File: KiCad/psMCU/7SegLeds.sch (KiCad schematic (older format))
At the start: 14 parts

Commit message: First Schematic Draft done.
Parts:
- removed D? (x6): LED, Diode_SMD:D_0603_1608Metric, symbol Device:LED_Small
- added D34, D35, D37, D38, D39, D40: LED_7seg, NoRef_Footprints:D_0402_1005Metric_NoRef, symbol Device:LED_Small
- D36: renamed from D?; value LED -> LED_7seg; footprint Diode_SMD:D_0603_1608Metric -> NoRef_Footprints:D_0402_1005Metric_NoRef
- R36, R37, R38, R39, R40, R41, R42: renamed from R?; footprint Resistor_SMD:R_0603_1608Metric -> NoRef_Footprints:R_0603_1608Metric
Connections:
- net GND: now also D34.1 (K), D35.1 (K), D37.1 (K), D38.1 (K), D39.1 (K), D40.1 (K)
- net at R37.1: now also D35.2 (A)
- net at R41.1: now also D39.2 (A)
- net at R40.1: now also D38.2 (A)
- net at R36.1: now also D34.2 (A)
- net at R39.1: now also D37.2 (A)
- net at R42.1: now also D40.2 (A)
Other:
- moved on the sheet: R360

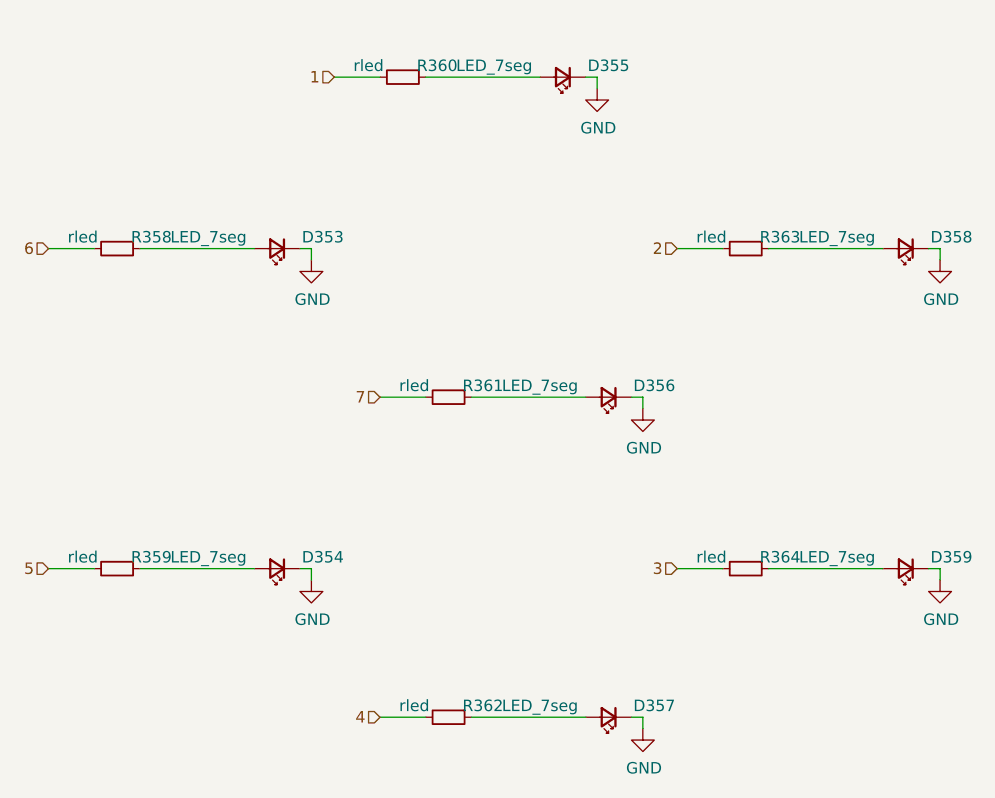
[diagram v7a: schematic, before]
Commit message: Reworked ref. location in schematic.
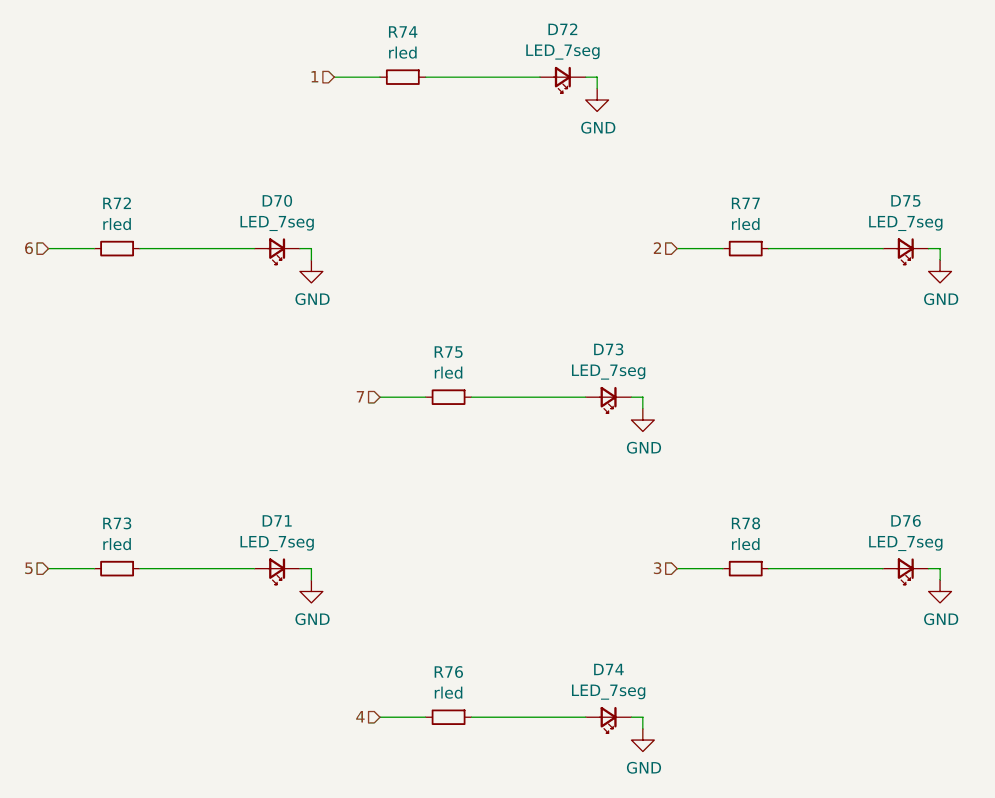
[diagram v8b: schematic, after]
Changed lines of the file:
@@
 $Descr A4 11693 8268
 encoding utf-8
-Sheet 82 110
+Sheet 19 110
 Title "psMCU"
 Date ""
@@
 AR Path="/5F607AA2/6046BFE9/61AA9AC0/607AED25" Ref="#PWR0512"  Part="1"
 AR Path="/5F607AA2/6046BFE9/61AA9AC7/607AED25" Ref="#PWR0526"  Part="1"
-F 0 "#PWR01202" H 6550 2000 50  0001 C CNN
+F 0 "#PWR0346" H 6550 2000 50  0001 C CNN
 F 1 "GND" H 6555 2077 50  0000 C CNN
 F 2 "" H 6550 2250 50  0001 C CNN
@@
 AR Path="/5F607AA2/6046BFE9/61AA9AC0/607AED30" Ref="R133"  Part="1"
 AR Path="/5F607AA2/6046BFE9/61AA9AC7/607AED30" Ref="R147"  Part="1"
-F 0 "R361" V 5850 3750 50  0000 C CNN
-F 1 "rled" V 5850 3450 50  0000 C CNN
+F 0 "R75" V 5704 3600 50  0000 C CNN
+F 1 "rled" V 5795 3600 50  0000 C CNN
 F 2 "NoRef_Footprints:R_0603_1608Metric" H 5900 3600 50  0001 C CNN
 F 3 "~" H 5900 3600 50  0001 C CNN
@@
 AR Path="/5F607AA2/6046BFE9/61AA9AC0/607AED32" Ref="R136"  Part="1"
 AR Path="/5F607AA2/6046BFE9/61AA9AC7/607AED32" Ref="R150"  Part="1"
-F 0 "R364" V 7150 4500 50  0000 C CNN
-F 1 "rled" V 7150 4200 50  0000 C CNN
+F 0 "R78" V 7004 4350 50  0000 C CNN
+F 1 "rled" V 7095 4350 50  0000 C CNN
 F 2 "NoRef_Footprints:R_0603_1608Metric" H 7200 4350 50  0001 C CNN
 F 3 "~" H 7200 4350 50  0001 C CNN
@@
 AR Path="/5F607AA2/6046BFE9/61AA9AC0/607AED35" Ref="R134"  Part="1"
 AR Path="/5F607AA2/6046BFE9/61AA9AC7/607AED35" Ref="R148"  Part="1"
-F 0 "R362" V 5850 5150 50  0000 C CNN
-F 1 "rled" V 5850 4850 50  0000 C CNN
+F 0 "R76" V 5704 5000 50  0000 C CNN
+F 1 "rled" V 5795 5000 50  0000 C CNN
 F 2 "NoRef_Footprints:R_0603_1608Metric" H 5900 5000 50  0001 C CNN
 F 3 "~" H 5900 5000 50  0001 C CNN
@@
 AR Path="/5F607AA2/6046BFE9/61AA9AC0/607AED37" Ref="R130"  Part="1"
 AR Path="/5F607AA2/6046BFE9/61AA9AC7/607AED37" Ref="R144"  Part="1"
-F 0 "R358" V 4400 3100 50  0000 C CNN
-F 1 "rled" V 4400 2800 50  0000 C CNN
+F 0 "R72" V 4254 2950 50  0000 C CNN
+F 1 "rled" V 4345 2950 50  0000 C CNN
 F 2 "NoRef_Footprints:R_0603_1608Metric" H 4450 2950 50  0001 C CNN
 F 3 "~" H 4450 2950 50  0001 C CNN
@@
 AR Path="/5F607AA2/6046BFE9/61AA9AC0/6039674B" Ref="R131"  Part="1"
 AR Path="/5F607AA2/6046BFE9/61AA9AC7/6039674B" Ref="R145"  Part="1"
-F 0 "R359" V 4400 4500 50  0000 C CNN
-F 1 "rled" V 4400 4200 50  0000 C CNN
+F 0 "R73" V 4254 4350 50  0000 C CNN
+F 1 "rled" V 4345 4350 50  0000 C CNN
 F 2 "NoRef_Footprints:R_0603_1608Metric" H 4450 4350 50  0001 C CNN
 F 3 "~" H 4450 4350 50  0001 C CNN
@@
 AR Path="/5F607AA2/6046BFE9/61AA9AC0/607AED24" Ref="D127"  Part="1"
 AR Path="/5F607AA2/6046BFE9/61AA9AC7/607AED24" Ref="D141"  Part="1"
-F 0 "D355" H 6200 2150 50  0000 C CNN
-F 1 "LED_7seg" H 6700 2150 50  0000 C CNN
+F 0 "D72" H 6400 1993 50  0000 C CNN
+F 1 "LED_7seg" H 6400 2084 50  0000 C CNN
 F 2 "NoRef_Footprints:D_0402_1005Metric_NoRef" V 6400 2200 50  0001 C CNN
 F 3 "~" V 6400 2200 50  0001 C CNN
@@
 AR Path="/5F607AA2/6046BFE9/61AA9AC0/607AED2A" Ref="R132"  Part="1"
 AR Path="/5F607AA2/6046BFE9/61AA9AC7/607AED2A" Ref="R146"  Part="1"
-F 0 "R360" V 5650 2350 50  0000 C CNN
-F 1 "rled" V 5650 2050 50  0000 C CNN
+F 0 "R74" V 5504 2200 50  0000 C CNN
+F 1 "rled" V 5595 2200 50  0000 C CNN
 F 2 "NoRef_Footprints:R_0603_1608Metric" H 5700 2200 50  0001 C CNN
 F 3 "~" H 5700 2200 50  0001 C CNN
@@
 AR Path="/5F607AA2/6046BFE9/61AA9AC0/603D3ABF" Ref="R135"  Part="1"
 AR Path="/5F607AA2/6046BFE9/61AA9AC7/603D3ABF" Ref="R149"  Part="1"
-F 0 "R363" V 7150 3100 50  0000 C CNN
-F 1 "rled" V 7150 2800 50  0000 C CNN
+F 0 "R77" V 7004 2950 50  0000 C CNN
+F 1 "rled" V 7095 2950 50  0000 C CNN
 F 2 "NoRef_Footprints:R_0603_1608Metric" H 7200 2950 50  0001 C CNN
 F 3 "~" H 7200 2950 50  0001 C CNN
@@
 AR Path="/5F607AA2/6046BFE9/61AA9AC0/607A1818" Ref="#PWR0515"  Part="1"
 AR Path="/5F607AA2/6046BFE9/61AA9AC7/607A1818" Ref="#PWR0529"  Part="1"
-F 0 "#PWR01205" H 8050 2750 50  0001 C CNN
+F 0 "#PWR0349" H 8050 2750 50  0001 C CNN
 F 1 "GND" H 8055 2827 50  0000 C CNN
 F 2 "" H 8050 3000 50  0001 C CNN
@@
 AR Path="/5F607AA2/6046BFE9/61AA9AC0/607A181E" Ref="D130"  Part="1"
 AR Path="/5F607AA2/6046BFE9/61AA9AC7/607A181E" Ref="D144"  Part="1"
-F 0 "D358" H 7700 2900 50  0000 C CNN
-F 1 "LED_7seg" H 8200 2900 50  0000 C CNN
+F 0 "D75" H 7900 2743 50  0000 C CNN
+F 1 "LED_7seg" H 7900 2834 50  0000 C CNN
 F 2 "NoRef_Footprints:D_0402_1005Metric_NoRef" V 7900 2950 50  0001 C CNN
 F 3 "~" V 7900 2950 50  0001 C CNN
@@
 AR Path="/5F607AA2/6046BFE9/61AA9AC0/607A1D19" Ref="#PWR0513"  Part="1"
 AR Path="/5F607AA2/6046BFE9/61AA9AC7/607A1D19" Ref="#PWR0527"  Part="1"
-F 0 "#PWR01203" H 6750 3400 50  0001 C CNN
+F 0 "#PWR0347" H 6750 3400 50  0001 C CNN
 F 1 "GND" H 6755 3477 50  0000 C CNN
 F 2 "" H 6750 3650 50  0001 C CNN
@@
 AR Path="/5F607AA2/6046BFE9/61AA9AC0/607A1D1F" Ref="D128"  Part="1"
 AR Path="/5F607AA2/6046BFE9/61AA9AC7/607A1D1F" Ref="D142"  Part="1"
-F 0 "D356" H 6400 3550 50  0000 C CNN
-F 1 "LED_7seg" H 6900 3550 50  0000 C CNN
+F 0 "D73" H 6600 3393 50  0000 C CNN
+F 1 "LED_7seg" H 6600 3484 50  0000 C CNN
 F 2 "NoRef_Footprints:D_0402_1005Metric_NoRef" V 6600 3600 50  0001 C CNN
 F 3 "~" V 6600 3600 50  0001 C CNN
@@
 AR Path="/5F607AA2/6046BFE9/61AA9AC0/607A250E" Ref="#PWR0516"  Part="1"
 AR Path="/5F607AA2/6046BFE9/61AA9AC7/607A250E" Ref="#PWR0530"  Part="1"
-F 0 "#PWR01206" H 8050 4150 50  0001 C CNN
+F 0 "#PWR0350" H 8050 4150 50  0001 C CNN
 F 1 "GND" H 8055 4227 50  0000 C CNN
 F 2 "" H 8050 4400 50  0001 C CNN
@@
 AR Path="/5F607AA2/6046BFE9/61AA9AC0/607A2514" Ref="D131"  Part="1"
 AR Path="/5F607AA2/6046BFE9/61AA9AC7/607A2514" Ref="D145"  Part="1"
-F 0 "D359" H 7700 4300 50  0000 C CNN
-F 1 "LED_7seg" H 8200 4300 50  0000 C CNN
+F 0 "D76" H 7900 4143 50  0000 C CNN
+F 1 "LED_7seg" H 7900 4234 50  0000 C CNN
 F 2 "NoRef_Footprints:D_0402_1005Metric_NoRef" V 7900 4350 50  0001 C CNN
 F 3 "~" V 7900 4350 50  0001 C CNN
@@
 AR Path="/5F607AA2/6046BFE9/61AA9AC0/607A2C81" Ref="#PWR0514"  Part="1"
 AR Path="/5F607AA2/6046BFE9/61AA9AC7/607A2C81" Ref="#PWR0528"  Part="1"
-F 0 "#PWR01204" H 6750 4800 50  0001 C CNN
+F 0 "#PWR0348" H 6750 4800 50  0001 C CNN
 F 1 "GND" H 6755 4877 50  0000 C CNN
 F 2 "" H 6750 5050 50  0001 C CNN
@@
 AR Path="/5F607AA2/6046BFE9/61AA9AC0/607A2C87" Ref="D129"  Part="1"
 AR Path="/5F607AA2/6046BFE9/61AA9AC7/607A2C87" Ref="D143"  Part="1"
-F 0 "D357" H 6400 4950 50  0000 C CNN
-F 1 "LED_7seg" H 6900 4950 50  0000 C CNN
+F 0 "D74" H 6600 4793 50  0000 C CNN
+F 1 "LED_7seg" H 6600 4884 50  0000 C CNN
 F 2 "NoRef_Footprints:D_0402_1005Metric_NoRef" V 6600 5000 50  0001 C CNN
 F 3 "~" V 6600 5000 50  0001 C CNN
@@
 AR Path="/5F607AA2/6046BFE9/61AA9AC0/607A3466" Ref="#PWR0511"  Part="1"
 AR Path="/5F607AA2/6046BFE9/61AA9AC7/607A3466" Ref="#PWR0525"  Part="1"
-F 0 "#PWR01201" H 5300 4150 50  0001 C CNN
+F 0 "#PWR0345" H 5300 4150 50  0001 C CNN
 F 1 "GND" H 5305 4227 50  0000 C CNN
 F 2 "" H 5300 4400 50  0001 C CNN
@@
 AR Path="/5F607AA2/6046BFE9/61AA9AC0/607A346C" Ref="D126"  Part="1"
 AR Path="/5F607AA2/6046BFE9/61AA9AC7/607A346C" Ref="D140"  Part="1"
-F 0 "D354" H 4950 4300 50  0000 C CNN
-F 1 "LED_7seg" H 5450 4300 50  0000 C CNN
+F 0 "D71" H 5150 4143 50  0000 C CNN
+F 1 "LED_7seg" H 5150 4234 50  0000 C CNN
 F 2 "NoRef_Footprints:D_0402_1005Metric_NoRef" V 5150 4350 50  0001 C CNN
 F 3 "~" V 5150 4350 50  0001 C CNN
@@
 AR Path="/5F607AA2/6046BFE9/61AA9AC0/607A42AB" Ref="#PWR0510"  Part="1"
 AR Path="/5F607AA2/6046BFE9/61AA9AC7/607A42AB" Ref="#PWR0524"  Part="1"
-F 0 "#PWR01200" H 5300 2750 50  0001 C CNN
+F 0 "#PWR0344" H 5300 2750 50  0001 C CNN
 F 1 "GND" H 5305 2827 50  0000 C CNN
 F 2 "" H 5300 3000 50  0001 C CNN
@@
 AR Path="/5F607AA2/6046BFE9/61AA9AC0/607A42B1" Ref="D125"  Part="1"
 AR Path="/5F607AA2/6046BFE9/61AA9AC7/607A42B1" Ref="D139"  Part="1"
-F 0 "D353" H 4950 2900 50  0000 C CNN
-F 1 "LED_7seg" H 5450 2900 50  0000 C CNN
+F 0 "D70" H 5150 2743 50  0000 C CNN
+F 1 "LED_7seg" H 5150 2834 50  0000 C CNN
 F 2 "NoRef_Footprints:D_0402_1005Metric_NoRef" V 5150 2950 50  0001 C CNN
 F 3 "~" V 5150 2950 50  0001 C CNN
